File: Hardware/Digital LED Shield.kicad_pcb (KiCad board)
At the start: 2 copper layers, 22 x 26.5 mm, 13 parts, among them J1 Conn_02x10_Odd_Even, J2 Conn_01x03_Male, J3 Barrel_Jack_MountingPin, J4 Conn_01x02_Female, U1 SN74LVC1T45DBV

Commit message: add protection
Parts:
- added D2: LM66100DCKR, LM66100DCKR:SOP65P210X110-6N, F.Cu at (155.8, 95.2)
- added G***: LOGO, LOGO, B.Cu at (133.8, 100.5)
- added IC1: LM431BCM3X_NOPB, LM431BCM3X:SOT95P237X95-3N, F.Cu at (150.9, 95.7)
- added IC2: LM66200DRLR, LM66200DRLR:SOTFL50P160X60-8N, F.Cu at (155.8, 92.5)
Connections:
- JP2 pad 2: +5VP -> +5VD

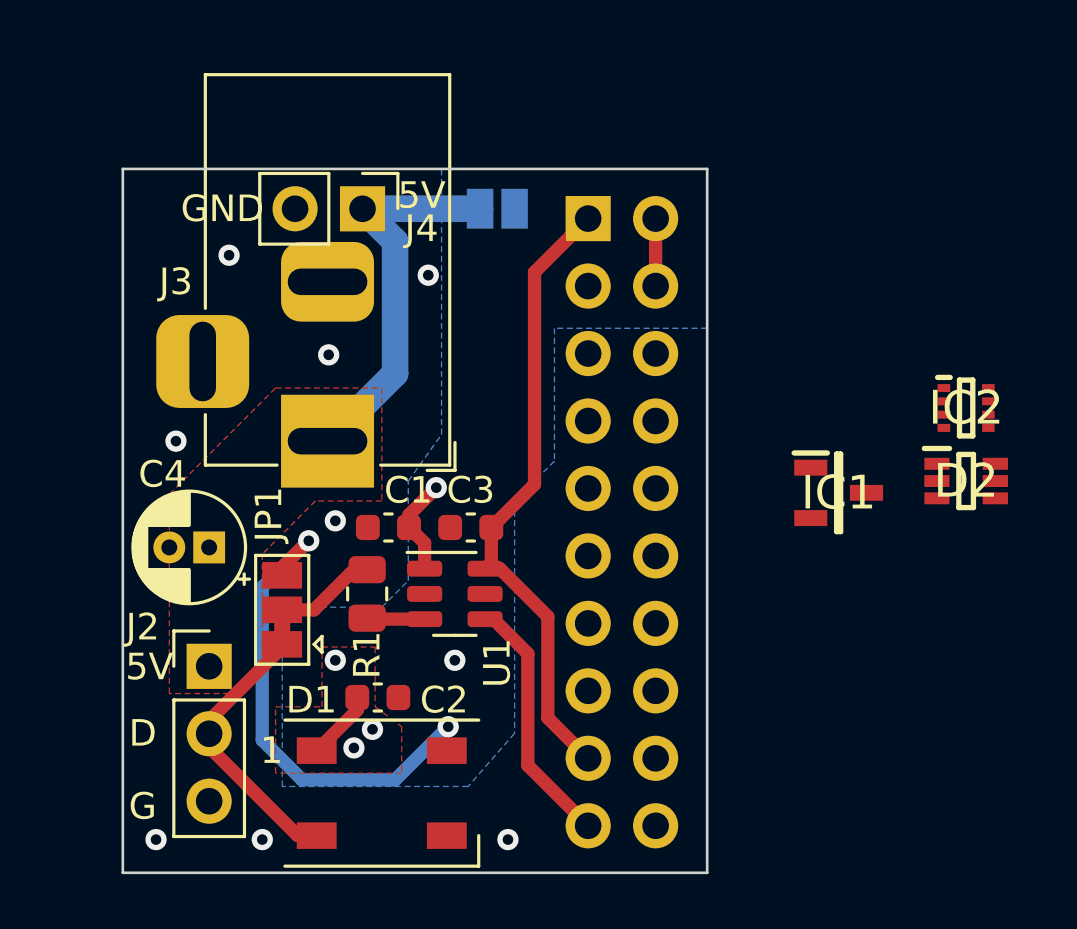
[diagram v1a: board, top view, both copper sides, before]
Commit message: Add protection and screw terminal
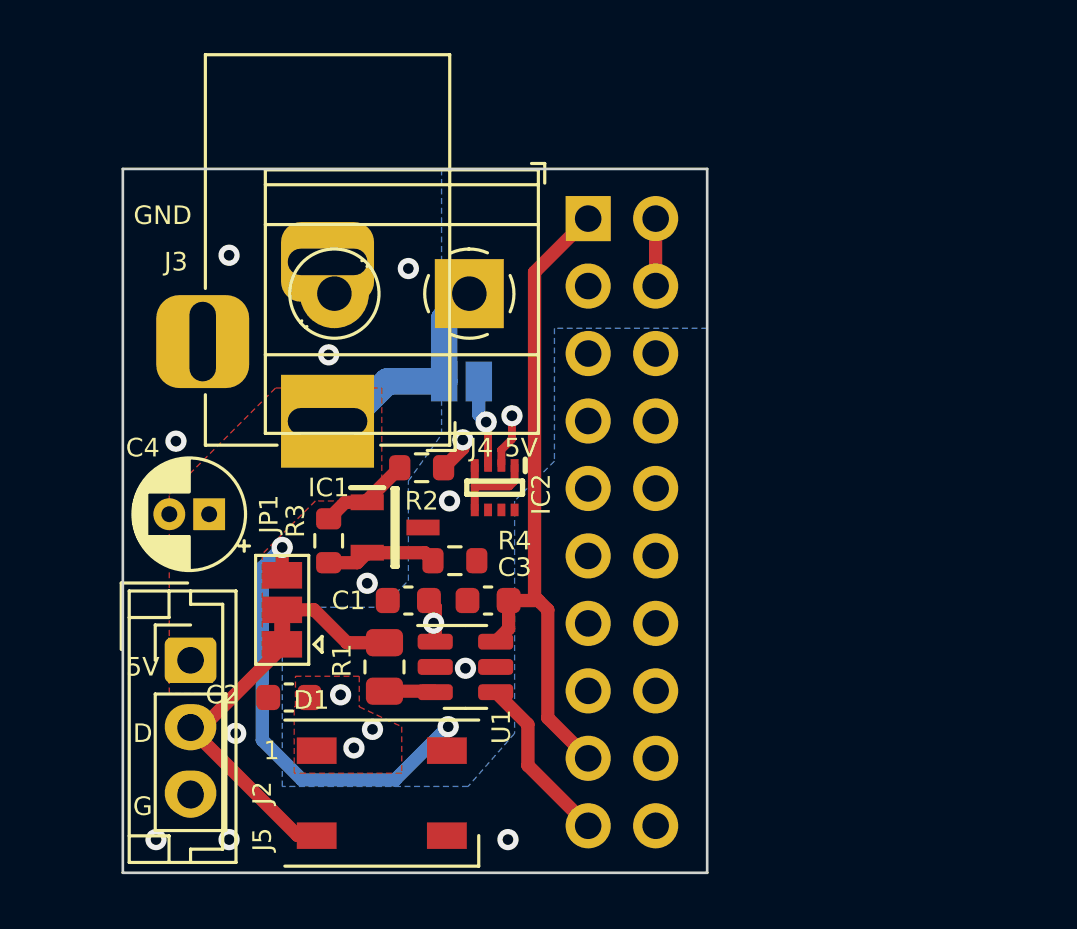
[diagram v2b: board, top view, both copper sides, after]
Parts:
- removed D2: LM66100DCKR, LM66100DCKR:SOP65P210X110-6N
- added J5: Conn_01x03_Male, Connector_JST:JST_EH_B3B-EH-A_1x03_P2.50mm_Vertical, F.Cu at (126.5, 102.0)
- added R2: R, Resistor_SMD:R_0603_1608Metric, F.Cu at (135.2, 94.8)
- added R3: 10k, Resistor_SMD:R_0603_1608Metric, F.Cu at (131.8, 97.5)
- added R4: 10k, Resistor_SMD:R_0603_1608Metric, F.Cu at (136.5, 98.2)
- J4: footprint Connector_PinHeader_2.54mm:PinHeader_1x02_P2.54mm_Vertical -> TerminalBlock_Phoenix:TerminalBlock_Phoenix_MKDS-1,5-2-5.08_1x02_P5.08mm_Horizontal
- moved IC2 18.0 mm to (138.0, 95.5), turned to -90 degrees
- moved IC1 16.8 mm to (134.2, 97.0)
- moved JP2 6.64 mm to (136.8, 91.5)
- moved J4 5.14 mm to (137.0, 88.2), turned to 180 degrees
- moved C2 3.35 mm to (130.2, 103.4), turned to 180 degrees
- moved C1 2.85 mm to (134.8, 99.8)
- moved C3 2.83 mm to (137.8, 99.8)
- moved R1 2.83 mm to (133.8, 102.2)
- moved U1 2.78 mm to (136.9, 102.2)
- moved C4 1.25 mm to (127.2, 96.5)
- moved J3 0.75 mm to (131.7, 93.0)
- moved J2 0.74 mm to (126.5, 102.0)
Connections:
- net Net-(D1-Pad2) renamed DOUT
- net Net-(D1-Pad4) renamed DIN
- IC1 pad 1: unconnected-(IC1-Pad1) -> Net-(IC1-Pad1)
- IC1 pad 2: unconnected-(IC1-Pad2) -> Net-(IC1-Pad2)
- IC1 pad 3: unconnected-(IC1-Pad3) -> GND
- IC2 pad 1: unconnected-(IC2-Pad1) -> GND
- IC2 pad 2: unconnected-(IC2-Pad2) -> +5VP
- IC2 pad 3: unconnected-(IC2-Pad3) -> +5VD
- IC2 pad 4: unconnected-(IC2-Pad4) -> GND
- IC2 pad 5: unconnected-(IC2-Pad5) -> GND
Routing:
- net +5V: track 14.7 -> 9.02 mm
- net Net-(IC1-Pad2): track 0.00 -> 4.20 mm
- net GND: track 0.00 -> 3.85 mm, vias 9 -> 11
- net Net-(IC1-Pad1): track 0.00 -> 3.52 mm
- net +5VD: track 0.00 -> 3.31 mm, vias 0 -> 1
- net /Data: track 9.57 -> 6.47 mm
- net DIN: track 18.4 -> 17.1 mm
- net +5VP: track 8.89 -> 7.57 mm, vias 4 -> 6
- net +3V3: track 23.9 -> 24.9 mm
- net Net-(JP1-Pad2): track 3.83 -> 4.36 mm
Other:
- board text added: "RPi Digital LED Shield V1"
- board text removed: "RPi Digital LED Shield"

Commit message: Add ordered Version V1
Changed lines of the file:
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@@
       (outputformat 1)
       (mirror false)
-      (drillshape 1)
+      (drillshape 0)
       (scaleselection 1)
       (outputdirectory "")
@@
     (fp_line (start -2.5 -1.6) (end -2.5 2.2) (layer "F.Fab") (width 0.1))
     (fp_line (start -2.91 2.61) (end -0.41 2.61) (layer "F.Fab") (width 0.1))
-    (pad "1" thru_hole roundrect (at 0 0 270) (size 1.7 1.95) (drill 0.95) (layers *.Cu *.Mask) (roundrect_rratio 0.147059)
+    (pad "1" thru_hole roundrect (at 0 0 270) (size 1.7 1.95) (drill 0.95) (layers *.Cu *.Mask) (roundrect_rratio 0.1470588235)
       (net 2 "+5V") (pinfunction "Pin_1") (pintype "passive"))
     (pad "2" thru_hole oval (at 2.5 0 270) (size 1.7 1.95) (drill 0.95) (layers *.Cu *.Mask)
@@
     (fp_line (start 1 -0.625) (end 1 0.625) (layer "F.Fab") (width 0.1))
     (fp_line (start 1 0.625) (end -1 0.625) (layer "F.Fab") (width 0.1))
-    (pad "1" smd roundrect locked (at -0.9125 0 270) (size 1.025 1.4) (layers "F.Cu" "F.Paste" "F.Mask") (roundrect_rratio 0.243902)
+    (pad "1" smd roundrect locked (at -0.9125 0 270) (size 1.025 1.4) (layers "F.Cu" "F.Paste" "F.Mask") (roundrect_rratio 0.243902439)
       (net 16 "Net-(JP1-Pad2)") (pintype "passive"))
-    (pad "2" smd roundrect locked (at 0.9125 0 270) (size 1.025 1.4) (layers "F.Cu" "F.Paste" "F.Mask") (roundrect_rratio 0.243902)
+    (pad "2" smd roundrect locked (at 0.9125 0 270) (size 1.025 1.4) (layers "F.Cu" "F.Paste" "F.Mask") (roundrect_rratio 0.243902439)
       (net 17 "Net-(R1-Pad2)") (pintype "passive"))
     (model "${KICAD6_3DMODEL_DIR}/Resistor_SMD.3dshapes/R_0805_2012Metric.wrl"

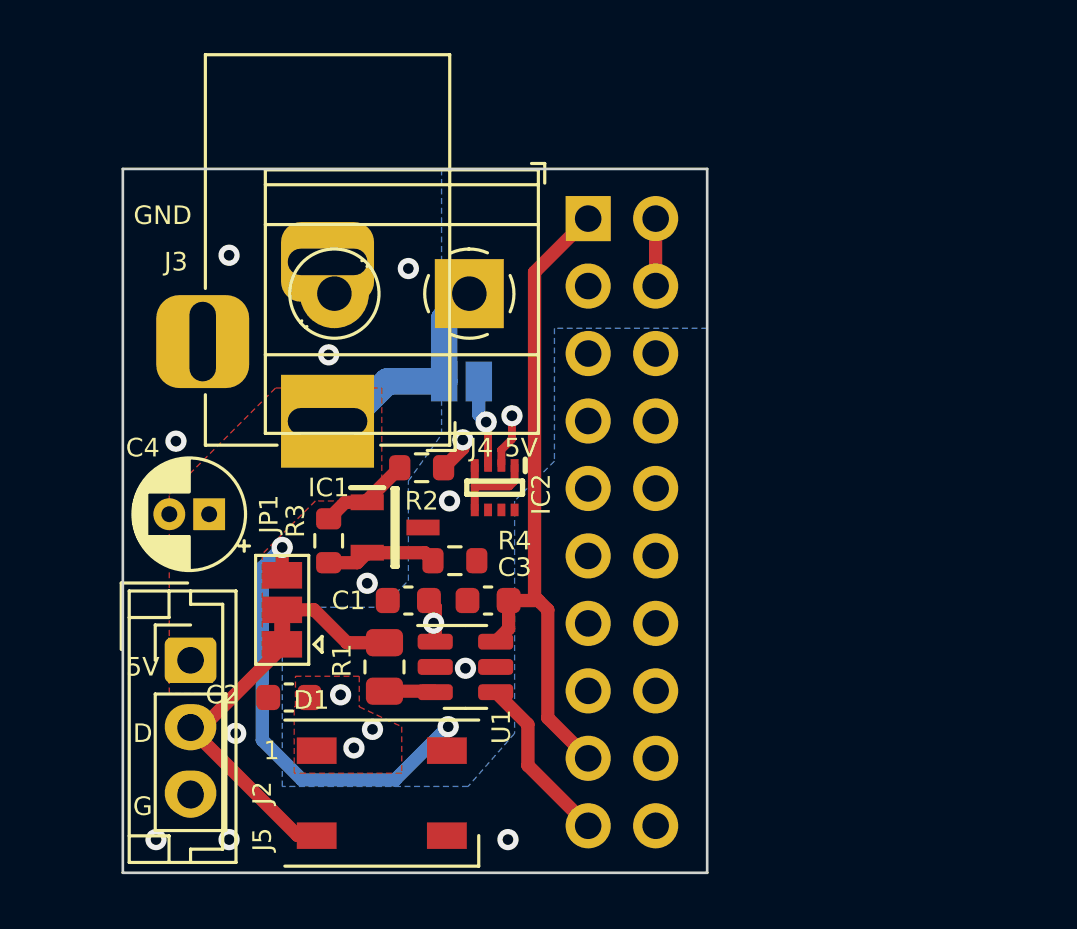
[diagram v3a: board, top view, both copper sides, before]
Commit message: change lm431 to TPS2420
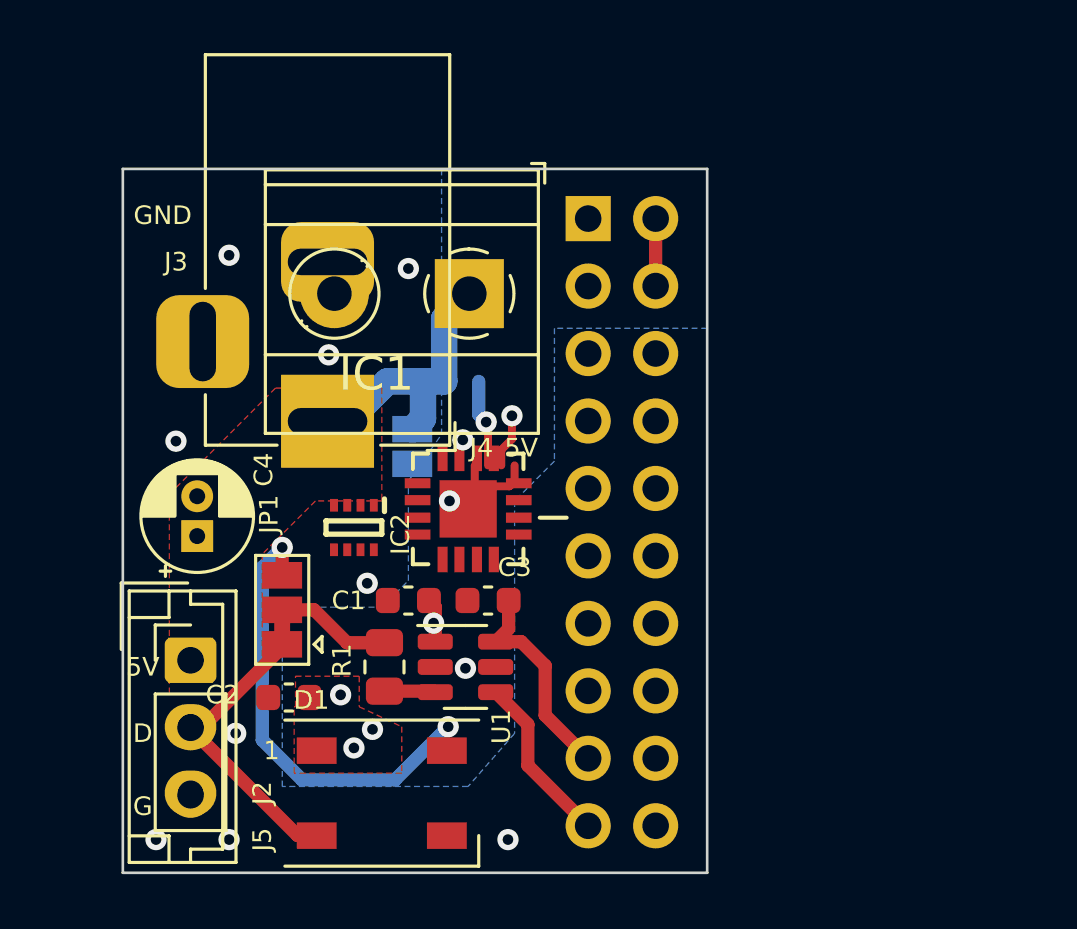
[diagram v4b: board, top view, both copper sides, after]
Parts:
- removed R2: R, Resistor_SMD:R_0603_1608Metric
- removed R3, R4: 10k, Resistor_SMD:R_0603_1608Metric
- C4: value C_Polarized -> 10uF
- IC1: value LM431BCM3X_NOPB -> TPS2420RSAT; footprint LM431BCM3X:SOT95P237X95-3N -> TPS2420RSAT:QFN65P400X400X100-17N
- moved IC2 5.51 mm to (132.7, 97.0)
- moved JP2 3.07 mm to (134.9, 94.0), turned to -90 degrees
- moved IC1 2.84 mm to (137.0, 96.3)
- moved C4 0.94 mm to (126.8, 97.3), turned to 90 degrees
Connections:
- IC1 pad 1: Net-(IC1-Pad1) -> +5VL
- IC1 pad 2: Net-(IC1-Pad2) -> +5VL
- IC1 pad 3: GND -> +5VL
- IC2 pad 2: +5VP -> +5VL
- J1 pad 1: +3V3 -> unconnected-(J1-Pad1)
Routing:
- net +3V3: track 24.9 -> 8.15 mm
- net unconnected-(IC1-Pad13): track 0.00 -> 5.34 mm, vias 0 -> 1
- net Net-(IC1-Pad2): track 4.20 -> 0.00 mm
- net Net-(IC1-Pad1): track 3.52 -> 0.00 mm
- net +5VP: track 7.57 -> 4.19 mm
- net +5VD: track 3.31 -> 0.00 mm, vias 1 -> 0
- net +5V: track 9.02 -> 11.0 mm
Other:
- board text added: "RPi Digital LED Shield V2"
- board text removed: "RPi Digital LED Shield V1"

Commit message: update sch and pcb
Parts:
- IC1: moved to B.Cu
- JP1: value Jumper_3_Bridged12 -> Jumper_3_Open; footprint Jumper:SolderJumper-3_P1.3mm_Bridged12_Pad1.0x1.5mm -> Jumper:SolderJumper-3_P1.3mm_Open_Pad1.0x1.5mm
- moved JP2 2.81 mm to (137.1, 92.2)
- moved IC2 0.92 mm to (132.0, 96.4), turned to 180 degrees
- moved J4 0.59 mm to (137.0, 87.6)
- moved JP1 0.56 mm to (130.6, 100.1)
- moved C2 0.46 mm to (130.7, 103.5)
- moved IC1 0.32 mm to (137.1, 96.6), turned to 180 degrees
- moved D1 0.30 mm to (133.8, 107.3)
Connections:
- IC2 pad 2: +5VL -> +5VP
- IC2 pad 3: +5VD -> +5VL
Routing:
- net unconnected-(IC1-Pad13): track 5.34 -> 0.00 mm, vias 1 -> 0
- net +5VP: track 4.19 -> 8.15 mm, vias 6 -> 11
- net GND: track 3.85 -> 0.00 mm, vias 11 -> 9
- net DIN: track 17.1 -> 19.6 mm
- net DOUT: track 10.8 -> 11.6 mm
- net +5V: track 11.0 -> 11.6 mm
- added copper zone on B.Cu, net +5VD

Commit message: update RPI Shield
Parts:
- moved G*** 4.71 mm to (133.5, 105.2)
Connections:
- IC1 pad 1: +5VL -> +5VD
- IC1 pad 10: +5VP -> +5VL
- IC1 pad 11: +5VP -> +5VL
- IC1 pad 12: unconnected-(IC1-Pad12) -> +5VL
- IC1 pad 16: unconnected-(IC1-Pad16) -> GND
- IC1 pad 2: +5VL -> +5VD
- IC1 pad 3: +5VL -> +5VD
- IC1 pad 4: +5VL -> +5VD
- IC1 pad 6: unconnected-(IC1-Pad6) -> GND
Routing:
- net +5VL: track 0.00 -> 1.28 mm, vias 0 -> 1
- net +5VP: track 8.15 -> 8.98 mm
- net GND: vias 9 -> 10
- added copper zone on B.Cu, net +5VL
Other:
- board text added: "5VD"
- board text added: "RPi Dig- ital LED Shield V2"
- board text removed: "RPi Digital LED Shield V2"

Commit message: Update Digital LED Shield.kicad_pcb
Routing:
- net +5VP: vias 11 -> 12
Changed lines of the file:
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@@
   (via (at 139.3 92) (size 0.8) (drill 0.4) (layers "F.Cu" "B.Cu") (free) (net 19))
   (via (at 135 93.3) (size 0.8) (drill 0.4) (layers "F.Cu" "B.Cu") (free) (net 19))
+  (via (at 132.3 98.3) (size 0.8) (drill 0.4) (layers "F.Cu" "B.Cu") (free) (net 19))
   (via (at 135.7 100.6) (size 0.8) (drill 0.4) (layers "F.Cu" "B.Cu") (free) (net 19))
   (via (at 133.4 104.6) (size 0.8) (drill 0.4) (layers "F.Cu" "B.Cu") (free) (net 19))

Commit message: add Gerber
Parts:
- added JP3: Jumper_2_Open, Jumper:SolderJumper-2_P1.3mm_Open_Pad1.0x1.5mm, B.Cu at (126.5, 109.2)
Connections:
- D1 pad 2: DOUT -> DOI
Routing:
- net DOI: track 0.00 -> 4.37 mm, vias 0 -> 1
- net DOUT: track 11.6 -> 11.1 mm
- net GND: vias 10 -> 8
